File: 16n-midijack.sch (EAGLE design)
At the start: 108 parts, among them J1 PJ302M, J10 PJ302M, J11 PJ302M, J12 PJ302M, J13 PJ302M, J14 PJ302M, J15 PJ302M, J16 PJ302M, J2 PJ302M, J3 PJ302M, J4 PJ302M, J5 PJ302M, J6 PJ302M, J7 PJ302M, J8 PJ302M, J9 PJ302M, U1 MCP6004_SMD, U2 MCP6004_SMD, U3 MCP6004_SMD, U4 MCP6004_SMD, U5 MCP6004_SMD, U6 MCP6004_SMD, U7 MCP6004_SMD, U8 MCP6004_SMD

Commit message: Remove legacy trace names.
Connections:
- new net N$300: R7.1, U1B.-IN, U1B.OUT
- new net N$301: R12.1, U1A.-IN, U1A.OUT
- new net N$302: R52.1, U2B.-IN, U2B.OUT
- new net N$303: R45.1, U2A.-IN, U2A.OUT
- new net N$304: R17.1, U3B.-IN, U3B.OUT
- new net N$305: R47.1, U3A.-IN, U3A.OUT
- new net N$306: R22.1, U4B.-IN, U4B.OUT
- new net N$307: R46.1, U4A.-IN, U4A.OUT
- new net N$308: R27.1, U5B.-IN, U5B.OUT
- new net N$309: R48.1, U5A.-IN, U5A.OUT
- new net N$310: R32.1, U6B.-IN, U6B.OUT
- new net N$311: R49.1, U6A.-IN, U6A.OUT
- new net N$312: R37.1, U7B.-IN, U7B.OUT
- new net N$313: R50.1, U7A.-IN, U7A.OUT
- new net N$314: R42.1, U8B.-IN, U8B.OUT
- new net N$315: R51.1, U8A.-IN, U8A.OUT
- net A0: no longer R7.1, U1B.-IN, U1B.OUT
- net A1: no longer R12.1, U1A.-IN, U1A.OUT
- net A10: no longer R32.1, U6B.-IN, U6B.OUT
- net A11: no longer R49.1, U6A.-IN, U6A.OUT
- net A12: no longer R37.1, U7B.-IN, U7B.OUT
- net A13: no longer R50.1, U7A.-IN, U7A.OUT
- net A14: no longer R42.1, U8B.-IN, U8B.OUT
- net A15: no longer R51.1, U8A.-IN, U8A.OUT
- net A2: no longer R52.1, U2B.-IN, U2B.OUT
- net A3: no longer R45.1, U2A.-IN, U2A.OUT
- net A4: no longer R17.1, U3B.-IN, U3B.OUT
- net A5: no longer R47.1, U3A.-IN, U3A.OUT
- net A6: no longer R22.1, U4B.-IN, U4B.OUT
- net A7: no longer R46.1, U4A.-IN, U4A.OUT
- net A8: no longer R27.1, U5B.-IN, U5B.OUT
- net A9: no longer R48.1, U5A.-IN, U5A.OUT

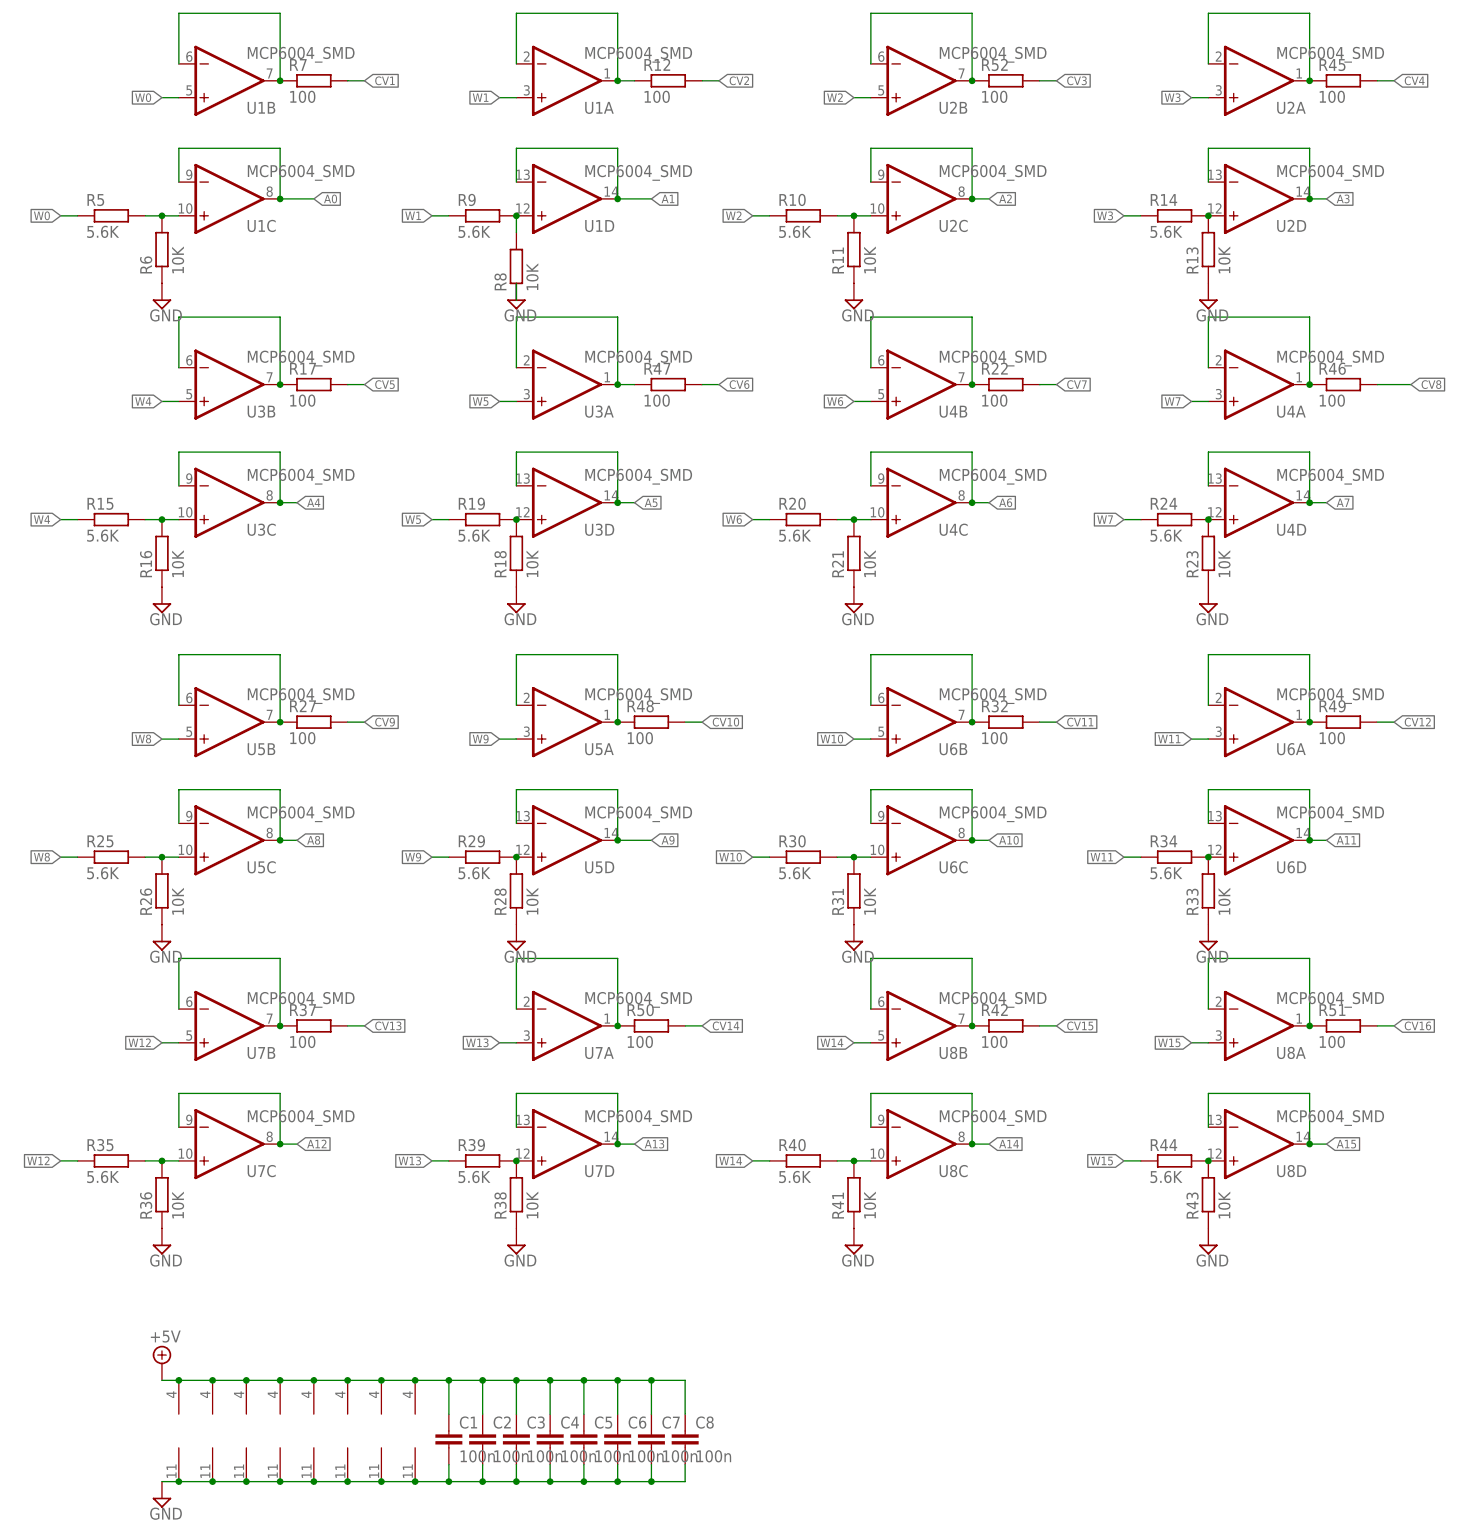
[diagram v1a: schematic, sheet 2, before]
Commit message: Fix gate positions.
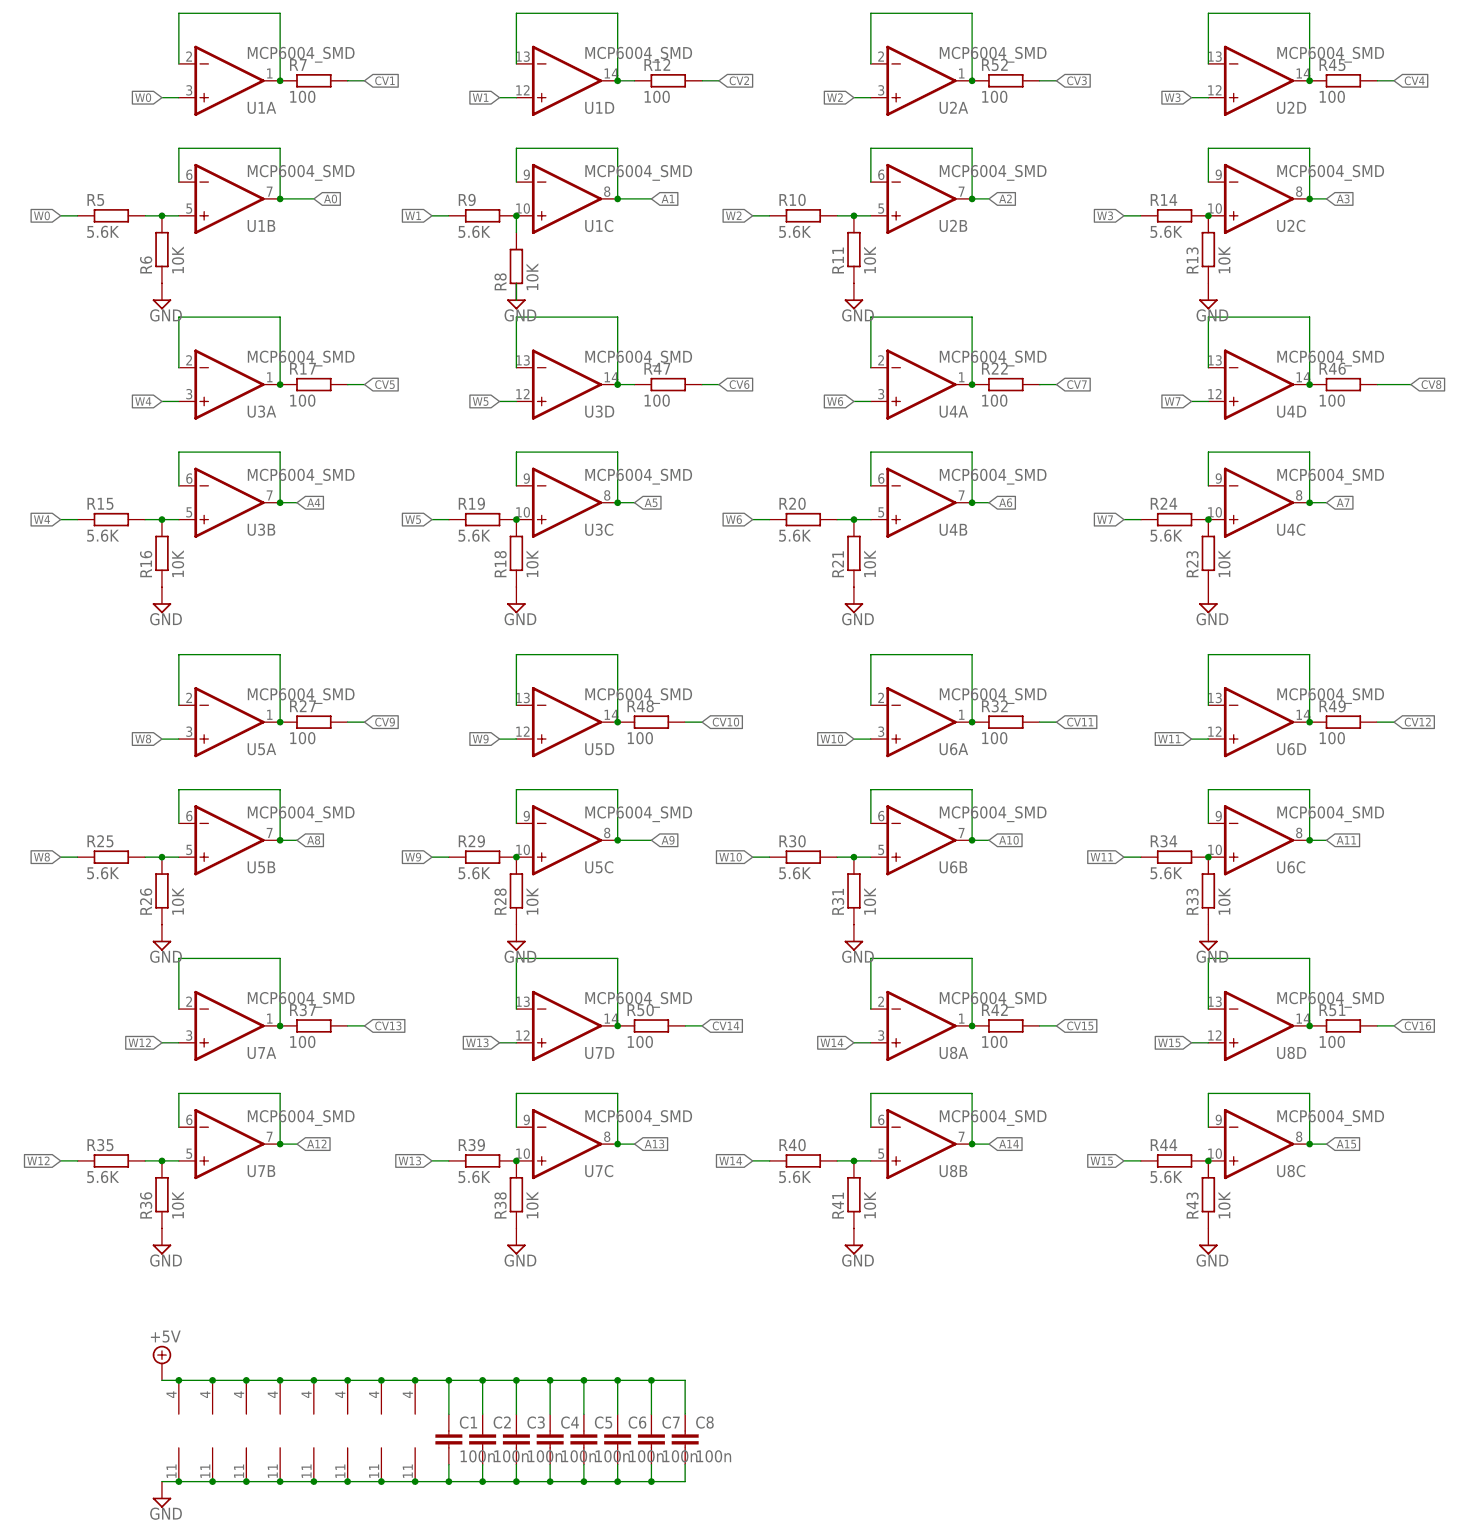
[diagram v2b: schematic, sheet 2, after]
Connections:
- net A0: now also U1B.-IN, U1B.OUT; no longer U1C.-IN, U1C.OUT
- net A1: now also U1C.-IN, U1C.OUT; no longer U1D.-IN, U1D.OUT
- net A10: now also U6B.-IN, U6B.OUT; no longer U6C.-IN, U6C.OUT
- net A11: now also U6C.-IN, U6C.OUT; no longer U6D.-IN, U6D.OUT
- net A12: now also U7B.-IN, U7B.OUT; no longer U7C.-IN, U7C.OUT
- net A13: now also U7C.-IN, U7C.OUT; no longer U7D.-IN, U7D.OUT
- net A14: now also U8B.-IN, U8B.OUT; no longer U8C.-IN, U8C.OUT
- net A15: now also U8C.-IN, U8C.OUT; no longer U8D.-IN, U8D.OUT
- net A2: now also U2B.-IN, U2B.OUT; no longer U2C.-IN, U2C.OUT
- net A3: now also U2C.-IN, U2C.OUT; no longer U2D.-IN, U2D.OUT
- net A4: now also U3B.-IN, U3B.OUT; no longer U3C.-IN, U3C.OUT
- net A5: now also U3C.-IN, U3C.OUT; no longer U3D.-IN, U3D.OUT
- net A6: now also U4B.-IN, U4B.OUT; no longer U4C.-IN, U4C.OUT
- net A7: now also U4C.-IN, U4C.OUT; no longer U4D.-IN, U4D.OUT
- net A8: now also U5B.-IN, U5B.OUT; no longer U5C.-IN, U5C.OUT
- net A9: now also U5C.-IN, U5C.OUT; no longer U5D.-IN, U5D.OUT
- net N$10: now also U1C.+IN; no longer U1D.+IN
- net N$12: now also U3B.+IN; no longer U3C.+IN
- net N$13: now also U3C.+IN; no longer U3D.+IN
- net N$15: now also U4B.+IN; no longer U4C.+IN
- net N$16: now also U4C.+IN; no longer U4D.+IN
- net N$18: now also U5B.+IN; no longer U5C.+IN
- net N$19: now also U5C.+IN; no longer U5D.+IN
- net N$21: now also U6B.+IN; no longer U6C.+IN
- net N$22: now also U6C.+IN; no longer U6D.+IN
- net N$24: now also U7B.+IN; no longer U7C.+IN
- net N$25: now also U7C.+IN; no longer U7D.+IN
- net N$27: now also U8B.+IN; no longer U8C.+IN
- net N$28: now also U8C.+IN; no longer U8D.+IN
- net N$300: now also U1A.-IN, U1A.OUT; no longer U1B.-IN, U1B.OUT
- net N$301: now also U1D.-IN, U1D.OUT; no longer U1A.-IN, U1A.OUT
- net N$302: now also U2A.-IN, U2A.OUT; no longer U2B.-IN, U2B.OUT
- net N$303: now also U2D.-IN, U2D.OUT; no longer U2A.-IN, U2A.OUT
- net N$304: now also U3A.-IN, U3A.OUT; no longer U3B.-IN, U3B.OUT
- net N$305: now also U3D.-IN, U3D.OUT; no longer U3A.-IN, U3A.OUT
- net N$306: now also U4A.-IN, U4A.OUT; no longer U4B.-IN, U4B.OUT
- net N$307: now also U4D.-IN, U4D.OUT; no longer U4A.-IN, U4A.OUT
- net N$308: now also U5A.-IN, U5A.OUT; no longer U5B.-IN, U5B.OUT
- net N$309: now also U5D.-IN, U5D.OUT; no longer U5A.-IN, U5A.OUT
- net N$310: now also U6A.-IN, U6A.OUT; no longer U6B.-IN, U6B.OUT
- net N$311: now also U6D.-IN, U6D.OUT; no longer U6A.-IN, U6A.OUT
- net N$312: now also U7A.-IN, U7A.OUT; no longer U7B.-IN, U7B.OUT
- net N$313: now also U7D.-IN, U7D.OUT; no longer U7A.-IN, U7A.OUT
- net N$314: now also U8A.-IN, U8A.OUT; no longer U8B.-IN, U8B.OUT
- net N$315: now also U8D.-IN, U8D.OUT; no longer U8A.-IN, U8A.OUT
- net N$6: now also U2B.+IN; no longer U2C.+IN
- net N$7: now also U2C.+IN; no longer U2D.+IN
- net N$9: now also U1B.+IN; no longer U1C.+IN
- net W0: now also U1A.+IN; no longer U1B.+IN
- net W1: now also U1D.+IN; no longer U1A.+IN
- net W10: now also U6A.+IN; no longer U6B.+IN
- net W11: now also U6D.+IN; no longer U6A.+IN
- net W12: now also U7A.+IN; no longer U7B.+IN
- net W13: now also U7D.+IN; no longer U7A.+IN
- net W14: now also U8A.+IN; no longer U8B.+IN
- net W15: now also U8D.+IN; no longer U8A.+IN
- net W2: now also U2A.+IN; no longer U2B.+IN
- net W3: now also U2D.+IN; no longer U2A.+IN
- net W4: now also U3A.+IN; no longer U3B.+IN
- net W5: now also U3D.+IN; no longer U3A.+IN
- net W6: now also U4A.+IN; no longer U4B.+IN
- net W7: now also U4D.+IN; no longer U4A.+IN
- net W8: now also U5A.+IN; no longer U5B.+IN
- net W9: now also U5D.+IN; no longer U5A.+IN
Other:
- moved on the sheet: U1A, U1B, U1C, U1D, U2A, U2B, U2C, U2D, U3A, U3B, U3C, U3D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

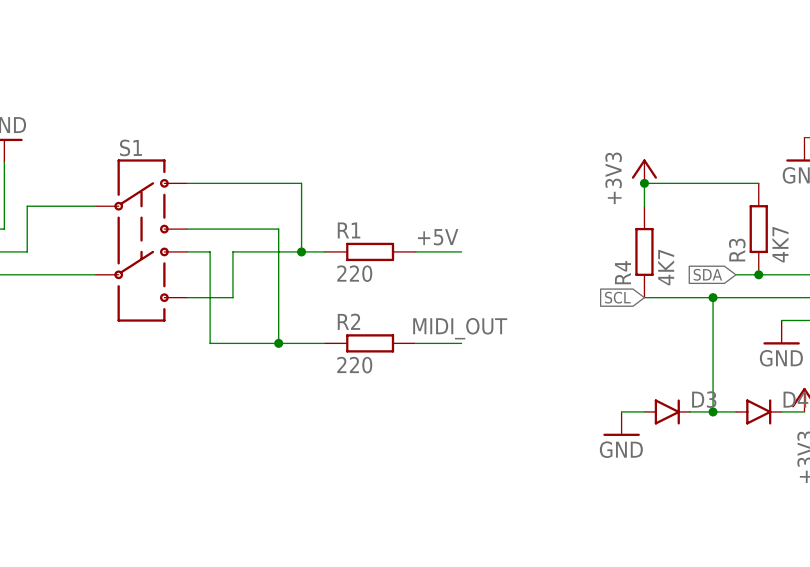
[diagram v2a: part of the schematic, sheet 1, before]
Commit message: MIDI positive voltage should be 3V3 for Teensy 3.x. Fixed that.
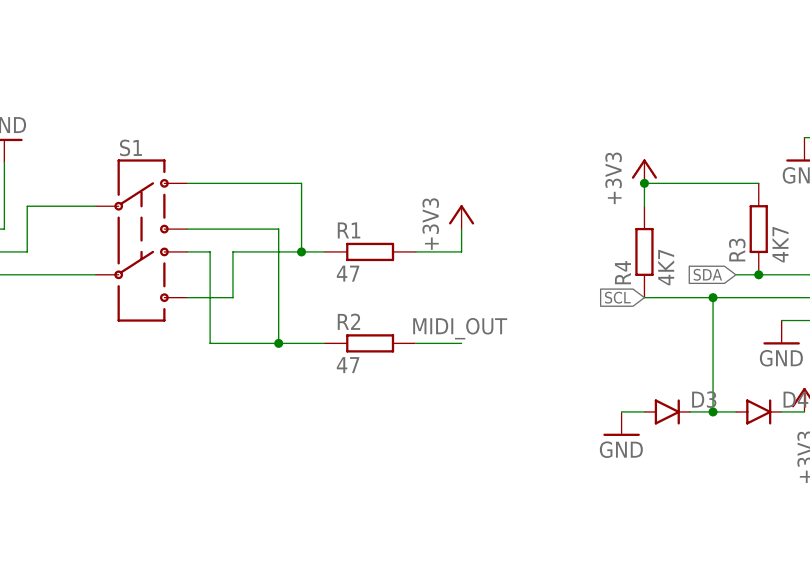
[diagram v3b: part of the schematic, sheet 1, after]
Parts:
- R1, R2: value 220 -> 47
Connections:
- net +3V3: now also R1.2
- net +5V: no longer R1.2
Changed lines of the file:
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@@
 <?xml version="1.0" encoding="utf-8"?>
 <!DOCTYPE eagle SYSTEM "eagle.dtd">
-<eagle version="8.4.1">
+<eagle version="8.4.3">
 <drawing>
 <settings>
@@
 <part name="GND16" library="supply1" deviceset="GND" device=""/>
 <part name="U$17" library="monome" deviceset="SLIDEPOT-ALPS-60MM" device=""/>
-<part name="R1" library="rcl" library_urn="urn:adsk.eagle:library:334" deviceset="R-EU_" device="R0805" package3d_urn="urn:adsk.eagle:package:23553/2" value="220"/>
-<part name="R2" library="rcl" library_urn="urn:adsk.eagle:library:334" deviceset="R-EU_" device="R0805" package3d_urn="urn:adsk.eagle:package:23553/2" value="220"/>
+<part name="R1" library="rcl" library_urn="urn:adsk.eagle:library:334" deviceset="R-EU_" device="R0805" package3d_urn="urn:adsk.eagle:package:23553/2" value="47"/>
+<part name="R2" library="rcl" library_urn="urn:adsk.eagle:library:334" deviceset="R-EU_" device="R0805" package3d_urn="urn:adsk.eagle:package:23553/2" value="47"/>
 <part name="JP1" library="SparkFun-Connectors" deviceset="AUDIO-JACK" device="PTH"/>
 <part name="GND17" library="supply1" deviceset="GND" device=""/>
@@
 <part name="R51" library="rcl" library_urn="urn:adsk.eagle:library:334" deviceset="R-EU_" device="R0805" package3d_urn="urn:adsk.eagle:package:23553/2" value="100"/>
 <part name="R52" library="rcl" library_urn="urn:adsk.eagle:library:334" deviceset="R-EU_" device="R0805" package3d_urn="urn:adsk.eagle:package:23553/2" value="100"/>
+<part name="+3V1" library="supply1" deviceset="+3V3" device=""/>
 </parts>
 <sheets>
@@
 <instance part="J16" gate="G$1" x="360.68" y="208.28"/>
 <instance part="SUPPLY33" gate="GND" x="353.06" y="203.2"/>
+<instance part="+3V1" gate="G$1" x="241.3" y="119.38"/>
 </instances>
 <busses>
@@
 <pinref part="+3V21" gate="G$1" pin="+3V3"/>
 </segment>
+<segment>
+<pinref part="R1" gate="G$1" pin="2"/>
+<wire x1="236.22" y1="114.3" x2="241.3" y2="114.3" width="0.1524" layer="91"/>
+<wire x1="241.3" y1="114.3" x2="241.3" y2="116.84" width="0.1524" layer="91"/>
+<pinref part="+3V1" gate="G$1" pin="+3V3"/>
+</segment>
 </net>
 <net name="A0" class="0">
@@
 </segment>
 <segment>
-<pinref part="R1" gate="G$1" pin="2"/>
-<wire x1="236.22" y1="114.3" x2="241.3" y2="114.3" width="0.1524" layer="91"/>
-<label x="236.22" y="115.062" size="1.778" layer="95"/>
-</segment>
-<segment>
